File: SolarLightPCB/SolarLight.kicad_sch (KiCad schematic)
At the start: 14 parts, among them J1 I2C, J2 Conn_01x06_Male, SW1 SW_Push, SW2 ON_OFF, U1 TP4056, U2 WeMos_D1_mini

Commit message: Update silkscreen
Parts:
- J2: value Conn_01x06_Male -> SPI
- SW1: value SW_Push -> Switch
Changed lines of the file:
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@@
     (in_bom yes) (on_board yes) (fields_autoplaced)
     (property "Reference" "J2" (id 0) (at 165.1 71.1199 0)
-      (effects (font (size 1.27 1.27)) (justify right))
-    )
-    (property "Value" "Conn_01x06_Male" (id 1) (at 165.1 73.6599 0)
+      (effects (font (size 1.27 1.27)) (justify right) hide)
+    )
+    (property "Value" "SPI" (id 1) (at 165.1 72.3899 0)
       (effects (font (size 1.27 1.27)) (justify right))
     )
@@
   (symbol (lib_id "Switch:SW_Push") (at 195.58 106.68 0) (unit 1)
     (in_bom yes) (on_board yes) (fields_autoplaced)
-    (property "Reference" "SW1" (id 0) (at 195.58 99.06 0))
-    (property "Value" "SW_Push" (id 1) (at 195.58 101.6 0))
+    (property "Reference" "SW1" (id 0) (at 195.58 99.06 0)
+      (effects (font (size 1.27 1.27)) hide)
+    )
+    (property "Value" "Switch" (id 1) (at 195.58 101.6 0))
     (property "Footprint" "Button_Switch_THT:SW_PUSH_6mm_H4.3mm" (id 2) (at 195.58 101.6 0)
       (effects (font (size 1.27 1.27)) hide)
@@
     (in_bom yes) (on_board yes) (fields_autoplaced)
     (property "Reference" "J1" (id 0) (at 196.342 80.0099 0)
-      (effects (font (size 1.27 1.27)) (justify left))
-    )
-    (property "Value" "I2C" (id 1) (at 196.342 82.5499 0)
+      (effects (font (size 1.27 1.27)) (justify left) hide)
+    )
+    (property "Value" "I2C" (id 1) (at 196.85 81.2799 0)
       (effects (font (size 1.27 1.27)) (justify left))
     )
@@
     )
     (path "/121c88c8-3029-42dd-a2f6-b1f466f1a87e"
-      (reference "J2") (unit 1) (value "Conn_01x06_Male") (footprint "Connector_PinHeader_2.54mm:PinHeader_1x06_P2.54mm_Vertical")
+      (reference "J2") (unit 1) (value "SPI") (footprint "Connector_PinHeader_2.54mm:PinHeader_1x06_P2.54mm_Vertical")
     )
     (path "/efe1edb9-34c9-473f-839b-20e06ddf294c"
@@
     )
     (path "/6c1b02c0-0815-4902-86e3-52c9345ae66e"
-      (reference "SW1") (unit 1) (value "SW_Push") (footprint "Button_Switch_THT:SW_PUSH_6mm_H4.3mm")
+      (reference "SW1") (unit 1) (value "Switch") (footprint "Button_Switch_THT:SW_PUSH_6mm_H4.3mm")
     )
     (path "/9f6d55fb-712b-4d9f-992e-0229120b6895"

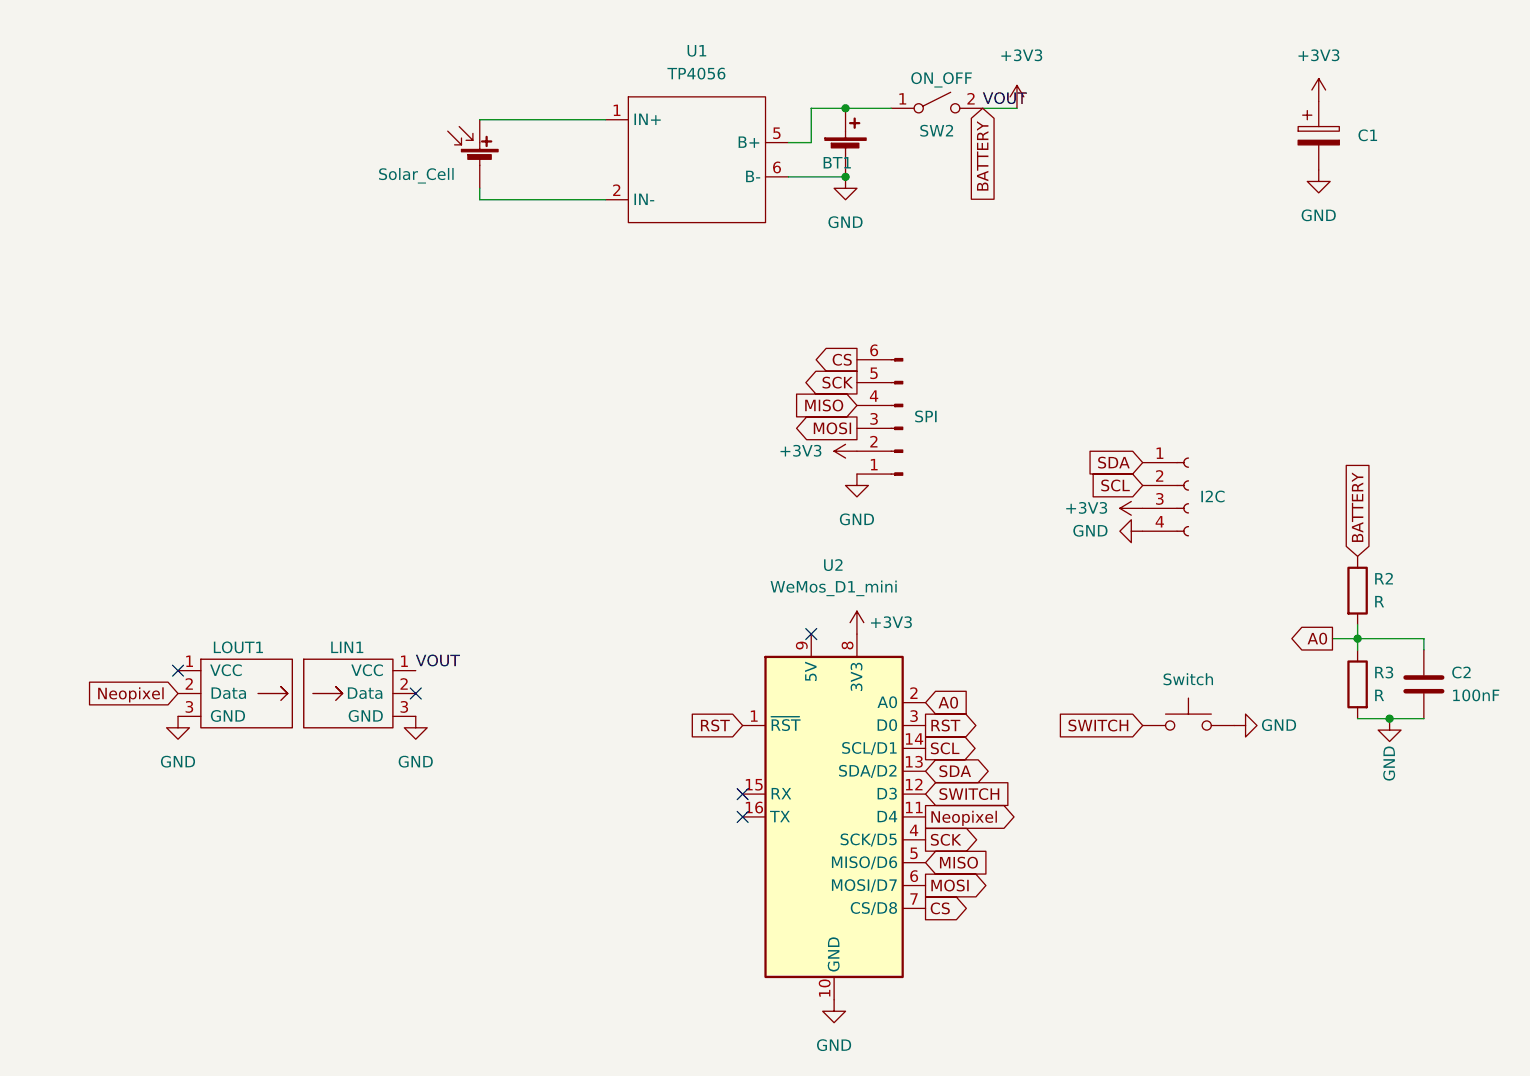
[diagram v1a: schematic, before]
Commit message: Added diode for reducing the voltage of the battery to ~3.3V
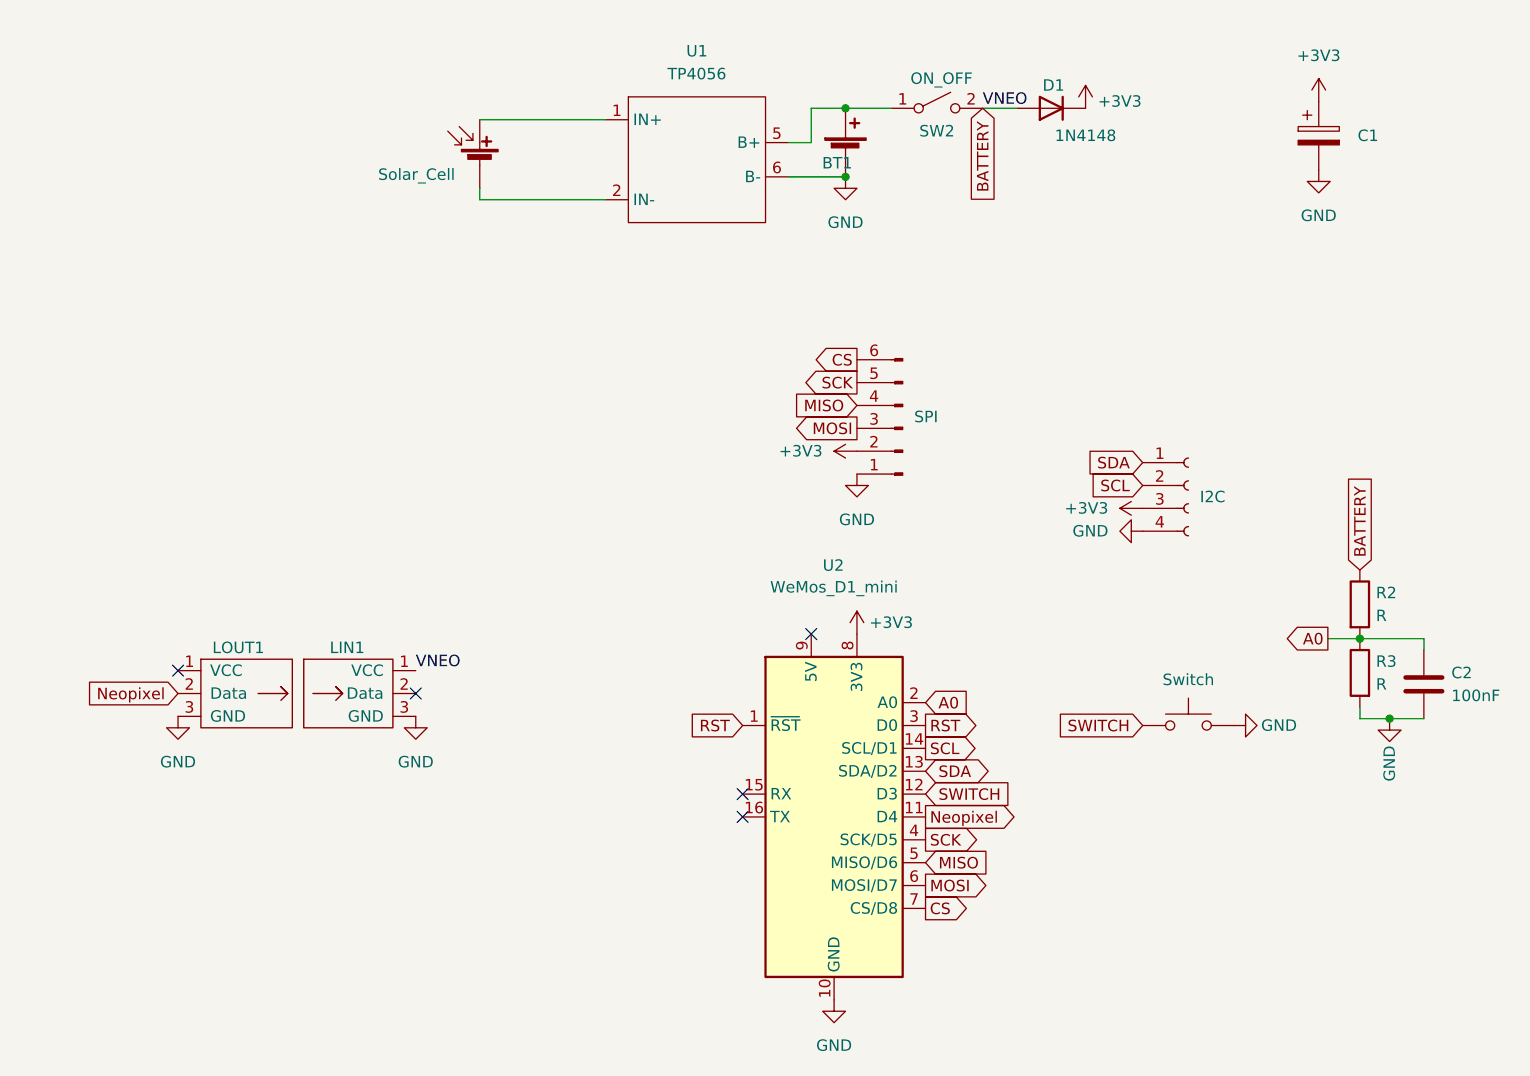
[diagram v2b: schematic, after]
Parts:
- added D1: 1N4148, Diode_THT:D_DO-35_SOD27_P7.62mm_Horizontal, symbol Diode:1N4148
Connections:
- net +3V3: now also D1.1 (K); no longer LIN1.1 (VCC), R2.1, SW2.2 (B)
- net A0: now also C2.1
- new net BATTERY: D1.2 (A), LIN1.1 (VCC), R2.1, SW2.2 (B)
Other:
- moved on the sheet: R2, R3
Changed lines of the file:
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@@
   (junction (at 217.932 105.918) (diameter 0) (color 0 0 0 0)
   )
-  (junction (at 214.376 97.028) (diameter 0) (color 0 0 0 0)
+  (junction (at 214.63 97.028) (diameter 0) (color 0 0 0 0)
   )
   (junction (at 157.48 45.72) (diameter 0) (color 0 0 0 0)
@@
     (stroke (width 0) (type default) (color 0 0 0 0))
   )
+  (wire (pts (xy 211.074 97.028) (xy 214.63 97.028))
+    (stroke (width 0) (type default) (color 0 0 0 0))
+  )
   (wire (pts (xy 116.84 48.26) (xy 116.84 46.99))
     (stroke (width 0) (type default) (color 0 0 0 0))
@@
     (stroke (width 0) (type default) (color 0 0 0 0))
   )
-  (wire (pts (xy 214.376 105.918) (xy 217.932 105.918))
-    (stroke (width 0) (type default) (color 0 0 0 0))
-  )
   (wire (pts (xy 153.67 38.1) (xy 153.67 41.91))
     (stroke (width 0) (type default) (color 0 0 0 0))
@@
     (stroke (width 0) (type default) (color 0 0 0 0))
   )
-  (wire (pts (xy 211.582 97.028) (xy 214.376 97.028))
-    (stroke (width 0) (type default) (color 0 0 0 0))
-  )
   (wire (pts (xy 217.932 105.918) (xy 221.742 105.918))
     (stroke (width 0) (type default) (color 0 0 0 0))
@@
     (stroke (width 0) (type default) (color 0 0 0 0))
   )
-  (wire (pts (xy 214.376 95.504) (xy 214.376 97.028))
-    (stroke (width 0) (type default) (color 0 0 0 0))
-  )
-  (wire (pts (xy 214.376 97.028) (xy 214.376 98.298))
-    (stroke (width 0) (type default) (color 0 0 0 0))
-  )
   (wire (pts (xy 116.84 39.37) (xy 130.81 39.37))
     (stroke (width 0) (type default) (color 0 0 0 0))
   )
-  (label "VOUT" (at 172.72 38.1 0)
+  (wire (pts (xy 214.63 104.648) (xy 214.63 105.918))
+    (stroke (width 0) (type default) (color 0 0 0 0))
+  )
+  (wire (pts (xy 214.63 105.918) (xy 217.932 105.918))
+    (stroke (width 0) (type default) (color 0 0 0 0))
+  )
+  (label "VNEO" (at 172.72 38.1 0)
     (effects (font (size 1.27 1.27)) (justify left bottom))
   )
-  (label "VOUT" (at 109.728 100.584 0)
+  (label "VNEO" (at 109.728 100.584 0)
     (effects (font (size 1.27 1.27)) (justify left bottom))
   )
@@
     )
   )
-  (global_label "A0" (shape output) (at 211.582 97.028 180) (fields_autoplaced)
-    (effects (font (size 1.27 1.27)) (justify right))
-    (property "Intersheet References" "${INTERSHEET_REFS}" (id 0) (at 206.8708 96.9486 0)
+  (global_label "A0" (shape output) (at 211.074 97.028 180) (fields_autoplaced)
+    (effects (font (size 1.27 1.27)) (justify right))
+    (property "Intersheet References" "${INTERSHEET_REFS}" (id 0) (at 206.3628 96.9486 0)
       (effects (font (size 1.27 1.27)) (justify right) hide)
     )
@@
     )
   )
-  (global_label "BATTERY" (shape input) (at 214.376 87.884 90) (fields_autoplaced)
-    (effects (font (size 1.27 1.27)) (justify left))
-    (property "Intersheet References" "${INTERSHEET_REFS}" (id 0) (at 214.2966 77.6695 90)
+  (global_label "BATTERY" (shape input) (at 214.63 89.408 90) (fields_autoplaced)
+    (effects (font (size 1.27 1.27)) (justify left))
+    (property "Intersheet References" "${INTERSHEET_REFS}" (id 0) (at 214.5506 79.1935 90)
       (effects (font (size 1.27 1.27)) (justify left) hide)
     )
@@
     (pin "2")
   )
-  (symbol (lib_id "power:+3V3") (at 176.53 38.1 0) (unit 1)
-    (in_bom yes) (on_board yes)
-    (property "Reference" "#PWR0104" (id 0) (at 176.53 41.91 0)
-      (effects (font (size 1.27 1.27)) hide)
-    )
-    (property "Value" "+3V3" (id 1) (at 177.038 32.258 0))
-    (property "Footprint" "" (id 2) (at 176.53 38.1 0)
-      (effects (font (size 1.27 1.27)) hide)
-    )
-    (property "Datasheet" "" (id 3) (at 176.53 38.1 0)
+  (symbol (lib_id "power:+3V3") (at 184.15 38.1 0) (unit 1)
+    (in_bom yes) (on_board yes)
+    (property "Reference" "#PWR0104" (id 0) (at 184.15 41.91 0)
+      (effects (font (size 1.27 1.27)) hide)
+    )
+    (property "Value" "+3V3" (id 1) (at 187.96 37.338 0))
+    (property "Footprint" "" (id 2) (at 184.15 38.1 0)
+      (effects (font (size 1.27 1.27)) hide)
+    )
+    (property "Datasheet" "" (id 3) (at 184.15 38.1 0)
       (effects (font (size 1.27 1.27)) hide)
     )
@@
     (pin "9")
   )
-  (symbol (lib_id "Device:R") (at 214.376 91.694 0) (unit 1)
-    (in_bom yes) (on_board yes) (fields_autoplaced)
-    (property "Reference" "R2" (id 0) (at 216.154 90.4239 0)
-      (effects (font (size 1.27 1.27)) (justify left))
-    )
-    (property "Value" "R" (id 1) (at 216.154 92.9639 0)
-      (effects (font (size 1.27 1.27)) (justify left))
-    )
-    (property "Footprint" "Resistor_THT:R_Axial_DIN0207_L6.3mm_D2.5mm_P7.62mm_Horizontal" (id 2) (at 212.598 91.694 90)
-      (effects (font (size 1.27 1.27)) hide)
-    )
-    (property "Datasheet" "~" (id 3) (at 214.376 91.694 0)
+  (symbol (lib_id "Diode:1N4148") (at 180.34 38.1 180) (unit 1)
+    (in_bom yes) (on_board yes)
+    (property "Reference" "D1" (id 0) (at 180.594 35.56 0))
+    (property "Value" "1N4148" (id 1) (at 184.15 41.148 0))
+    (property "Footprint" "Diode_THT:D_DO-35_SOD27_P7.62mm_Horizontal" (id 2) (at 180.34 33.655 0)
+      (effects (font (size 1.27 1.27)) hide)
+    )
+    (property "Datasheet" "https://assets.nexperia.com/documents/data-sheet/1N4148_1N4448.pdf" (id 3) (at 180.34 38.1 0)
+      (effects (font (size 1.27 1.27)) hide)
+    )
+    (pin "1")
+    (pin "2")
+  )
+  (symbol (lib_id "Device:R") (at 214.63 93.218 0) (unit 1)
+    (in_bom yes) (on_board yes) (fields_autoplaced)
+    (property "Reference" "R2" (id 0) (at 216.408 91.9479 0)
+      (effects (font (size 1.27 1.27)) (justify left))
+    )
+    (property "Value" "R" (id 1) (at 216.408 94.4879 0)
+      (effects (font (size 1.27 1.27)) (justify left))
+    )
+    (property "Footprint" "Resistor_THT:R_Axial_DIN0207_L6.3mm_D2.5mm_P7.62mm_Horizontal" (id 2) (at 212.852 93.218 90)
+      (effects (font (size 1.27 1.27)) hide)
+    )
+    (property "Datasheet" "~" (id 3) (at 214.63 93.218 0)
       (effects (font (size 1.27 1.27)) hide)
     )
@@
     (pin "2")
   )
-  (symbol (lib_id "Device:R") (at 214.376 102.108 0) (mirror y) (unit 1)
-    (in_bom yes) (on_board yes) (fields_autoplaced)
-    (property "Reference" "R3" (id 0) (at 216.154 100.8379 0)
+  (symbol (lib_id "Device:R") (at 214.63 100.838 0) (mirror y) (unit 1)
+    (in_bom yes) (on_board yes) (fields_autoplaced)
+    (property "Reference" "R3" (id 0) (at 216.408 99.5679 0)
       (effects (font (size 1.27 1.27)) (justify right))
     )
-    (property "Value" "R" (id 1) (at 216.154 103.3779 0)
+    (property "Value" "R" (id 1) (at 216.408 102.1079 0)
       (effects (font (size 1.27 1.27)) (justify right))
     )
-    (property "Footprint" "Resistor_THT:R_Axial_DIN0207_L6.3mm_D2.5mm_P7.62mm_Horizontal" (id 2) (at 216.154 102.108 90)
-      (effects (font (size 1.27 1.27)) hide)
-    )
-    (property "Datasheet" "~" (id 3) (at 214.376 102.108 0)
+    (property "Footprint" "Resistor_THT:R_Axial_DIN0207_L6.3mm_D2.5mm_P7.62mm_Horizontal" (id 2) (at 216.408 100.838 90)
+      (effects (font (size 1.27 1.27)) hide)
+    )
+    (property "Datasheet" "~" (id 3) (at 214.63 100.838 0)
       (effects (font (size 1.27 1.27)) hide)
     )
@@
       (reference "C2") (unit 1) (value "100nF") (footprint "Capacitor_THT:C_Disc_D5.0mm_W2.5mm_P5.00mm")
     )
+    (path "/d48d9258-1411-4a67-8f59-9447f2981510"
+      (reference "D1") (unit 1) (value "1N4148") (footprint "Diode_THT:D_DO-35_SOD27_P7.62mm_Horizontal")
+    )
     (path "/b014f64b-63d7-4679-a15c-8f4cf024b19d"
